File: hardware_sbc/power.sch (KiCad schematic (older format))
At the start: 56 parts, among them J6 Conn_01x02, J7 S2B-PH-K-S(LF)(SN), J8 Conn_01x01_Male, J9 0874380343, U10 MIC94164, U11 BQ29702, U12 BQ27426, U14 CSD85302L, U5 MP2636GR-P, U6 NCP133AMX150TCG

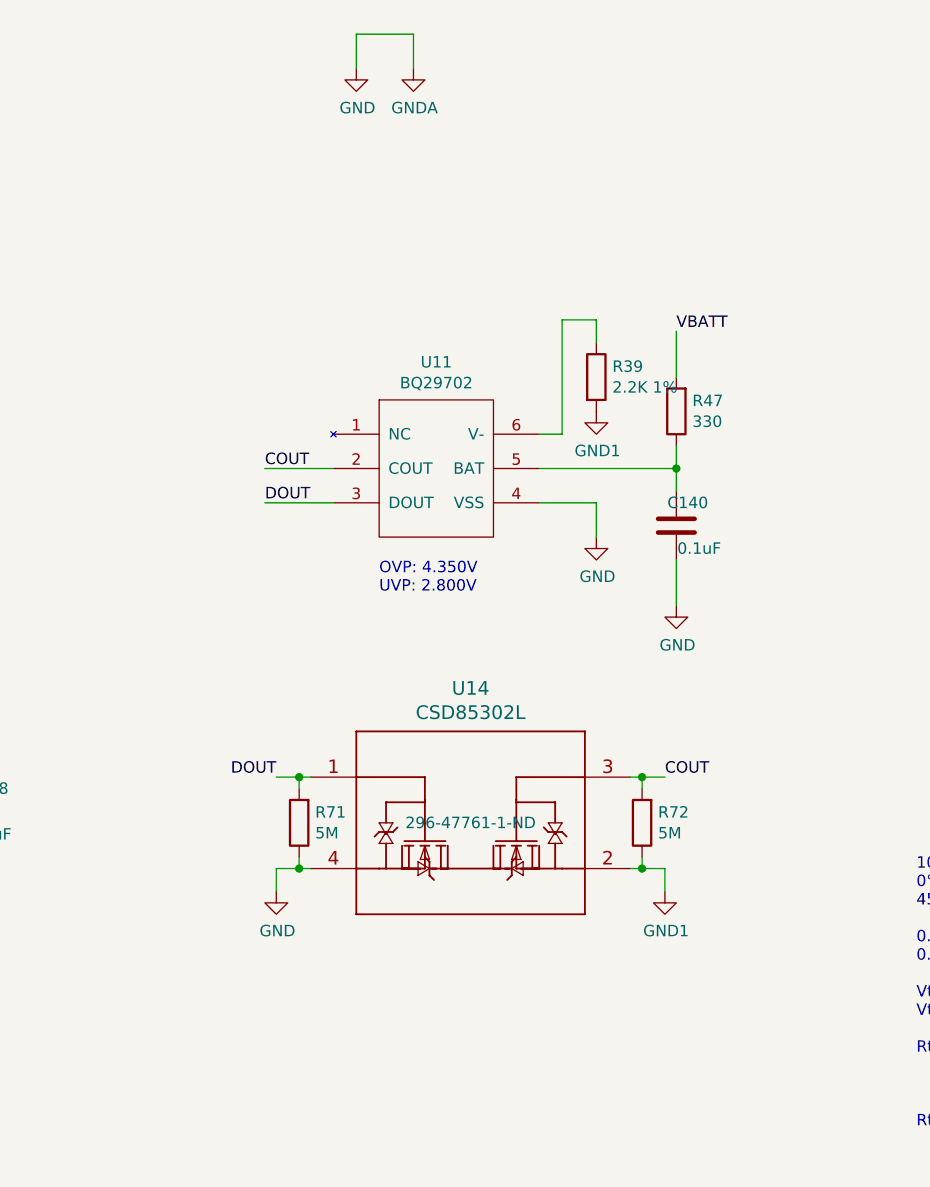
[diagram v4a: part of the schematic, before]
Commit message: Fixes for battery cutoff circuit (again)
The DOUT side is supposed to be connected to the battery, and COUT
to the board facing side. This is now correct.
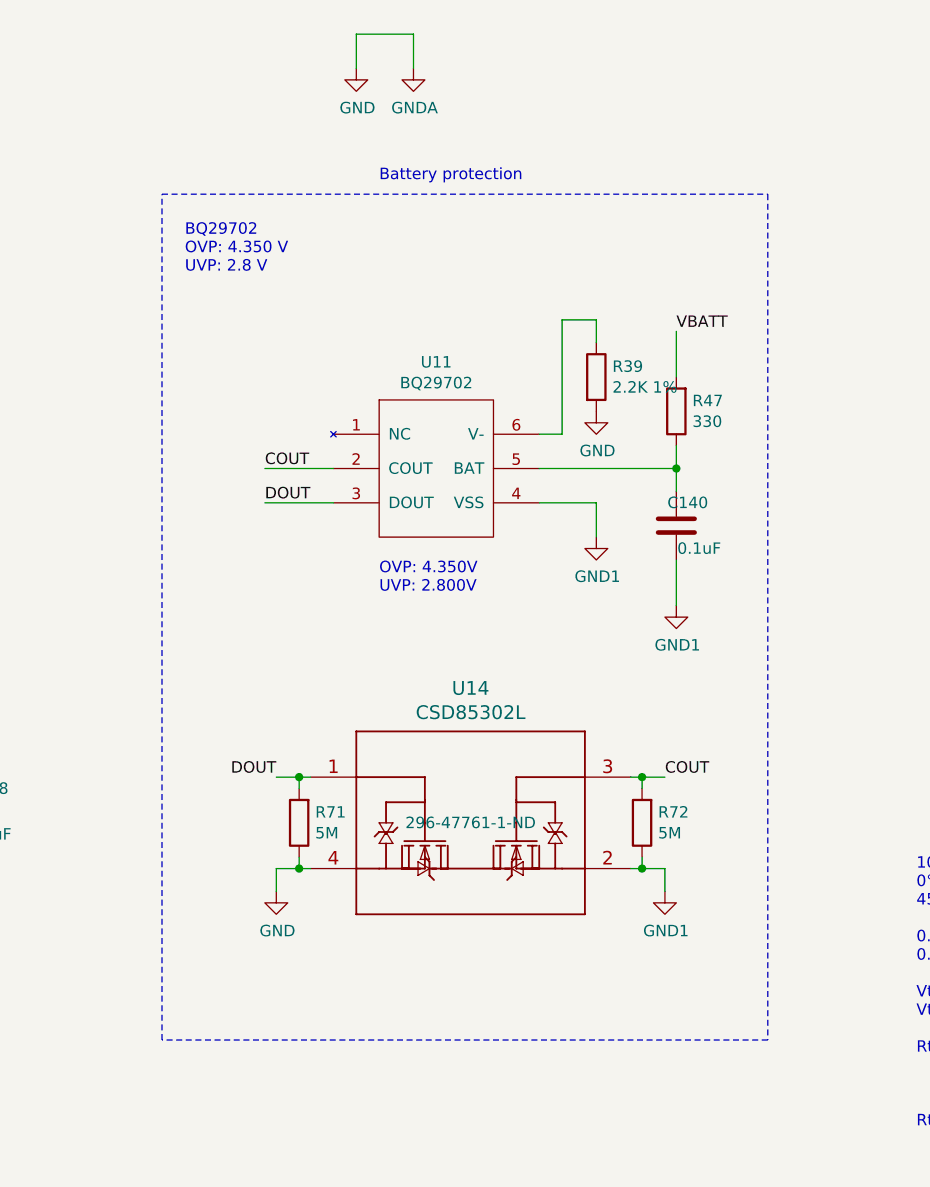
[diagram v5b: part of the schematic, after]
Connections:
- net GND: now also R39.2; no longer C140.2, U11.4 (VSS)
- net GND1: now also C140.2, U11.4 (VSS); no longer R39.2
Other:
- note added: "BQ29702\nOVP: 4.350 V\nUVP: 2.8 V"
- note added: "Battery protection"
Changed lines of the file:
@@
 L power:GND #PWR0231
 U 1 1 5EAD5FA4
-P 7850 7600
-F 0 "#PWR0231" H 7850 7350 50  0001 C CNN
-F 1 "GND" H 7855 7427 50  0000 C CNN
-F 2 "" H 7850 7600 50  0001 C CNN
-F 3 "" H 7850 7600 50  0001 C CNN
-	1    7850 7600
+P 7500 6750
+F 0 "#PWR0231" H 7500 6500 50  0001 C CNN
+F 1 "GND" H 7505 6577 50  0000 C CNN
+F 2 "" H 7500 6750 50  0001 C CNN
+F 3 "" H 7500 6750 50  0001 C CNN
+	1    7500 6750
 	1    0    0    -1
 $EndComp
@@
 Wire Wire Line
 	7500 7300 7500 7150
-$Comp
-L power:GND #PWR0232
-U 1 1 5EA9508B
-P 7500 7300
-F 0 "#PWR0232" H 7500 7050 50  0001 C CNN
-F 1 "GND" H 7505 7127 50  0000 C CNN
-F 2 "" H 7500 7300 50  0001 C CNN
-F 3 "" H 7500 7300 50  0001 C CNN
-	1    7500 7300
-	1    0    0    -1
-$EndComp
 Text Notes 6550 7550 0    50   ~ 0
 OVP: 4.350V\nUVP: 2.800V
@@
 L power:GND1 #PWR0158
 U 1 1 6057737F
-P 7500 6750
-F 0 "#PWR0158" H 7500 6500 50  0001 C CNN
-F 1 "GND1" H 7505 6577 50  0000 C CNN
-F 2 "" H 7500 6750 50  0001 C CNN
-F 3 "" H 7500 6750 50  0001 C CNN
-	1    7500 6750
+P 7850 7600
+F 0 "#PWR0158" H 7850 7350 50  0001 C CNN
+F 1 "GND1" H 7855 7427 50  0000 C CNN
+F 2 "" H 7850 7600 50  0001 C CNN
+F 3 "" H 7850 7600 50  0001 C CNN
+	1    7850 7600
 	1    0    0    -1
 $EndComp
@@
 Wire Wire Line
 	9150 2400 9900 2400
+$Comp
+L power:GND1 #PWR?
+U 1 1 60590093
+P 7500 7300
+F 0 "#PWR?" H 7500 7050 50  0001 C CNN
+F 1 "GND1" H 7505 7127 50  0000 C CNN
+F 2 "" H 7500 7300 50  0001 C CNN
+F 3 "" H 7500 7300 50  0001 C CNN
+	1    7500 7300
+	1    0    0    -1
+$EndComp
+Wire Notes Line
+	5600 5800 8250 5800
+Wire Notes Line
+	8250 5800 8250 9500
+Wire Notes Line
+	8250 9500 5600 9500
+Wire Notes Line
+	5600 9500 5600 5800
+Text Notes 5700 6150 0    50   ~ 0
+BQ29702\nOVP: 4.350 V\nUVP: 2.8 V
+Text Notes 6550 5750 0    50   ~ 0
+Battery protection
 $EndSCHEMATC
